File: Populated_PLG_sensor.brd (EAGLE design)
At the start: 160 x 100 mm, 24 parts, among them CON1 USB_MOLEX_0480372200, CON2 4_PIN_HEADER, J1 MICRO-SD_CARD_SOCKET, SW1 SPST_TACT-KMR2, SW2 SPST_TACT-KMR2, SW3 SPST_TACT-KMR2, SW4 SPST_TACT-KMR2

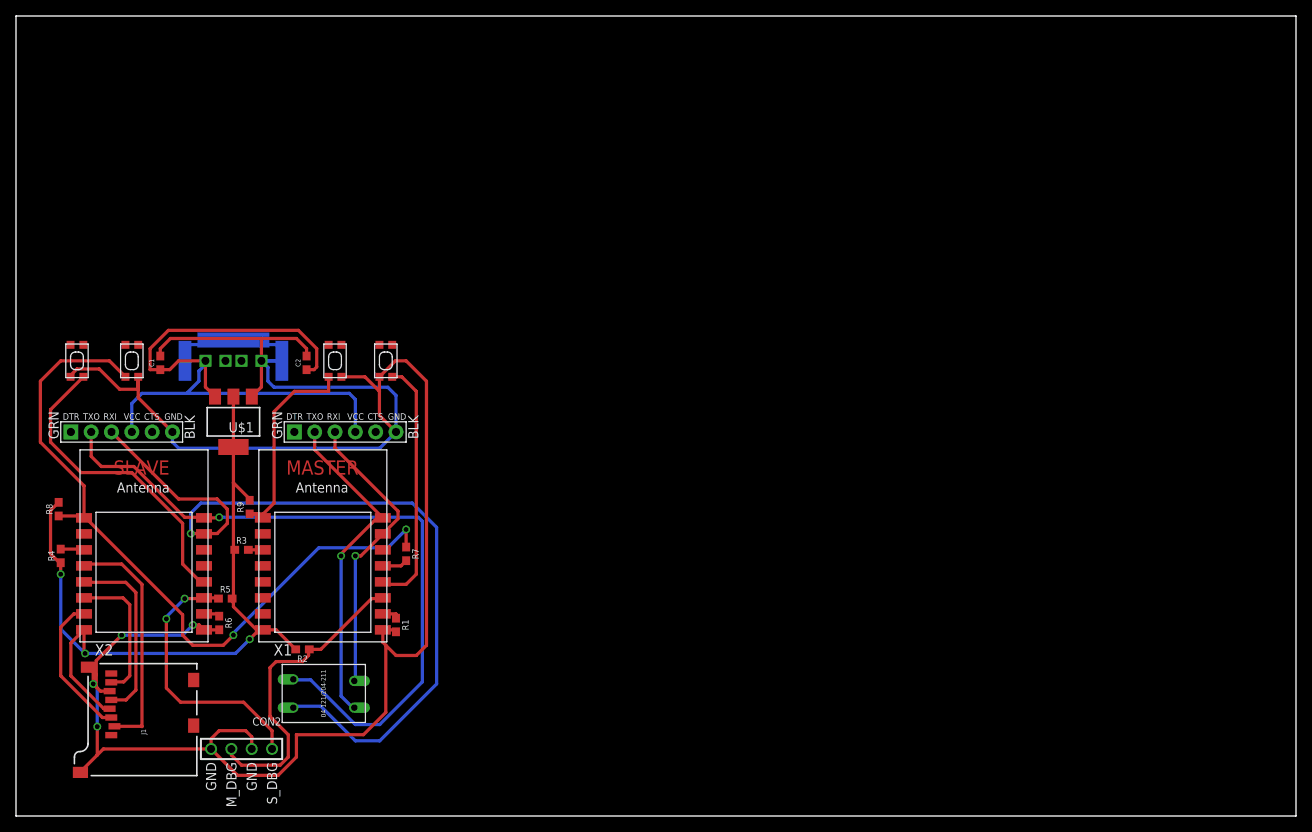
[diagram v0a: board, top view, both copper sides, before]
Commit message: Added logo, button & switch labels
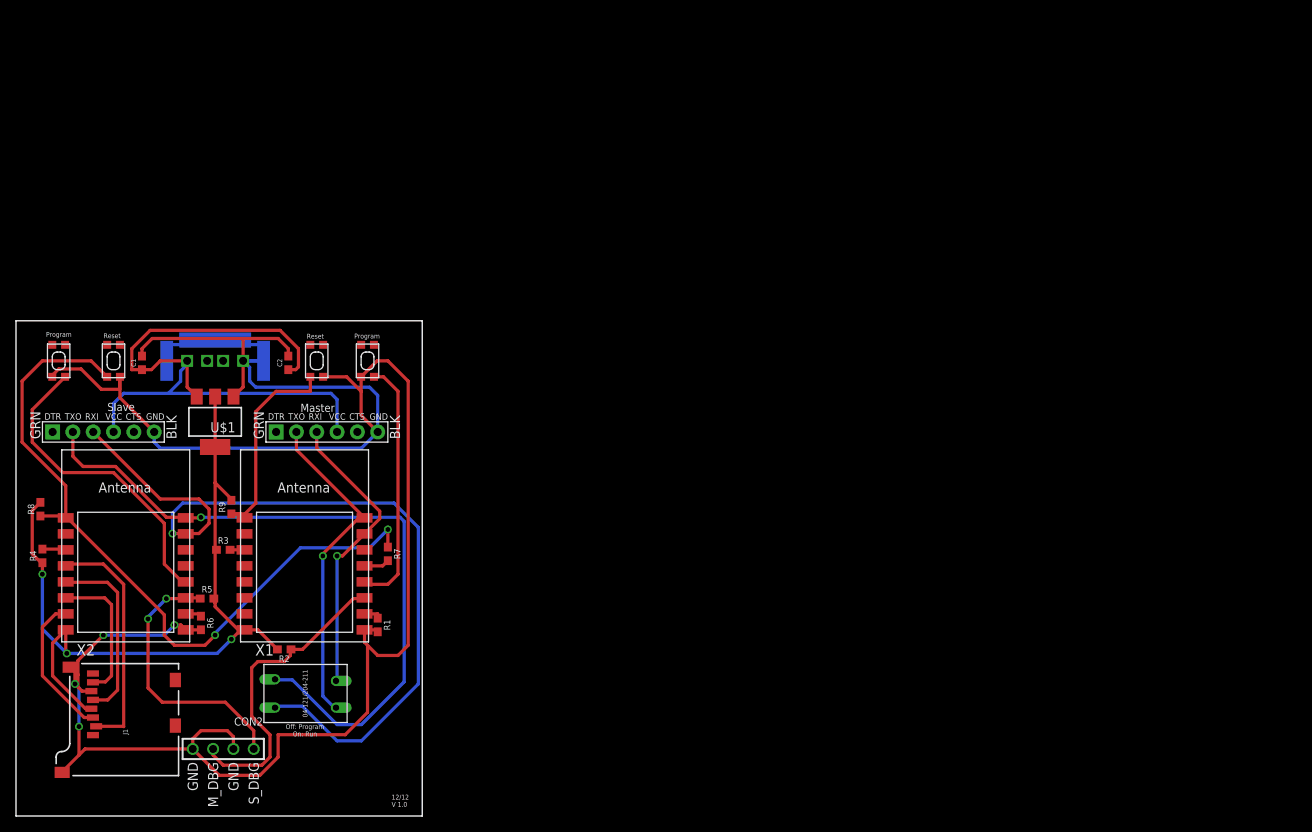
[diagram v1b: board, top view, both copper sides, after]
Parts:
- moved C2 2.29 mm to (34.0, 56.6)
- moved CON1 2.29 mm to (24.9, 56.9)
- moved DPST1 2.29 mm to (31.0, 11.7)
- moved J1 2.29 mm to (20.3, 19.1)
- moved JP1 2.29 mm to (38.9, 48.0)
- moved R2 2.29 mm to (33.5, 20.8)
- moved R7 2.29 mm to (46.5, 32.8)
- moved R9 2.29 mm to (26.9, 38.6)
- moved SW1 2.29 mm to (43.9, 56.9)
- moved SW2 2.29 mm to (37.6, 56.9)
- moved U$1 2.29 mm to (24.9, 49.3)
- moved X1 2.29 mm to (36.1, 32.8)
- moved SW3 2.29 mm to (5.33, 56.9)
- moved R4 2.29 mm to (3.30, 32.5)
- moved C1 2.29 mm to (15.7, 56.6)
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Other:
- board size 160 x 100 mm -> 50.8 x 61.9 mm
- board text added: "12/12 V 1.0"
- board text added: "C:/Users/mckenneyc/Desktop/soofa logo.bmp"
- board text added: "Master"
- board text added: "Off: Program On: Run"
- board text added: "Program"
- board text added: "Reset"
- board text added: "Slave"
- board text removed: "MASTER"
- board text removed: "SLAVE"

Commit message: Fixed Clearance issue
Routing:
- net MASTER_RX: track 37.1 -> 38.5 mm
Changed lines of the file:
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@@
 <wire x1="37.592" y1="48.006" x2="37.592" y2="45.974" width="0.4064" layer="1"/>
 <wire x1="37.592" y1="45.974" x2="45.466" y2="38.1" width="0.4064" layer="1"/>
-<wire x1="45.466" y1="38.1" x2="45.466" y2="37.164" width="0.4064" layer="1"/>
-<wire x1="45.466" y1="37.164" x2="43.568" y2="35.266" width="0.4064" layer="1"/>
 <wire x1="39.998" y1="16.884" x2="40.132" y2="16.884" width="0.4064" layer="16"/>
 <wire x1="40.132" y1="16.884" x2="40.132" y2="32.512" width="0.4064" layer="16"/>
 <via x="40.132" y="32.512" extent="1-16" drill="0.6" shape="square"/>
 <wire x1="40.132" y1="32.512" x2="40.814" y2="32.512" width="0.4064" layer="1"/>
-<wire x1="40.814" y1="32.512" x2="43.568" y2="35.266" width="0.4064" layer="1"/>
+<wire x1="45.466" y1="38.1" x2="45.466" y2="36.078159375" width="0.4064" layer="1"/>
+<wire x1="45.466" y1="36.078159375" x2="44.63288125" y2="35.245040625" width="0.4064" layer="1"/>
+<wire x1="44.63288125" y1="35.245040625" x2="43.588959375" y2="35.245040625" width="0.4064" layer="1"/>
+<wire x1="43.588959375" y1="35.245040625" x2="43.568" y2="35.266" width="0.4064" layer="1"/>
+<wire x1="40.814" y1="32.512" x2="40.814" y2="33.671521875" width="0.4064" layer="1"/>
+<wire x1="40.814" y1="33.671521875" x2="42.377359375" y2="35.23488125" width="0.4064" layer="1"/>
+<wire x1="42.377359375" y1="35.23488125" x2="43.53688125" y2="35.23488125" width="0.4064" layer="1"/>
+<wire x1="43.53688125" y1="35.23488125" x2="43.568" y2="35.266" width="0.4064" layer="1"/>
 </signal>
 <signal name="SLAVE_TX">
